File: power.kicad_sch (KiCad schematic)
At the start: 17 parts, among them J1 Conn_01x02, U2 TPS563200

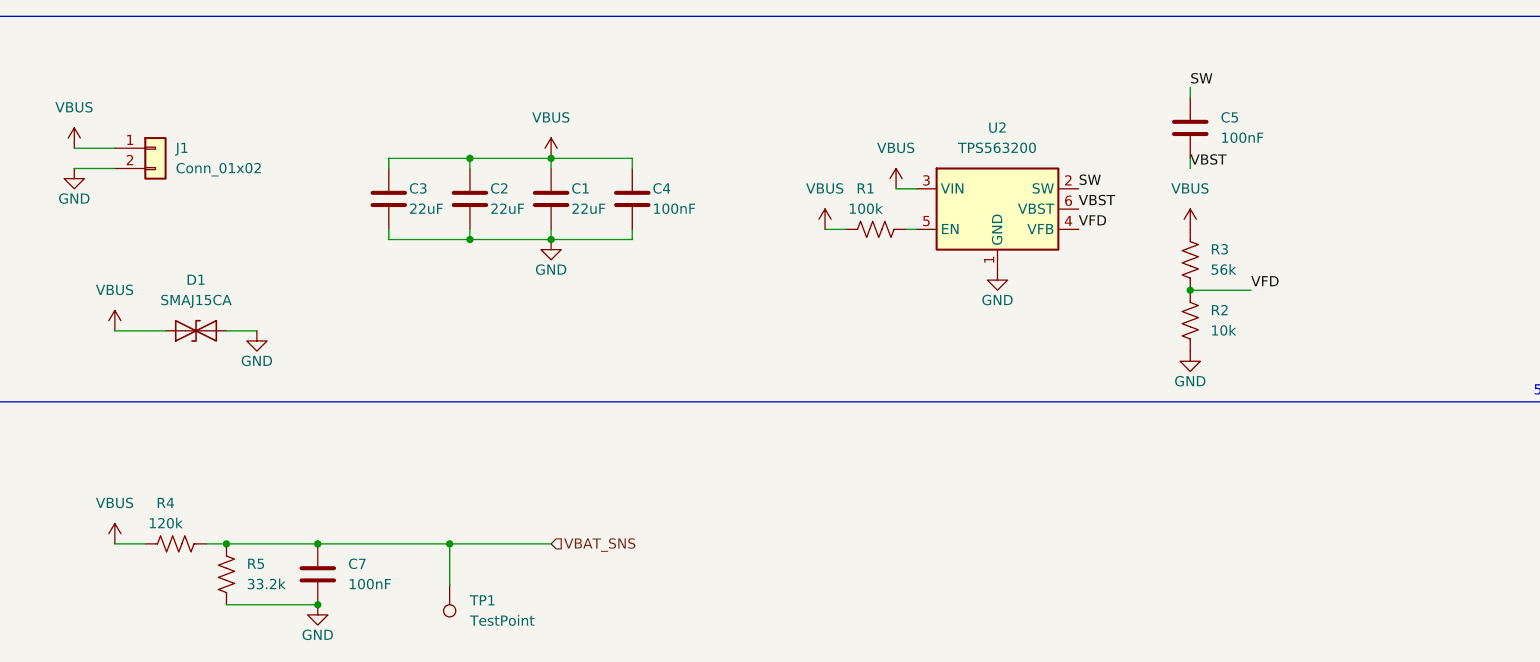
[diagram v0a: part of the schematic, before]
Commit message: fix power schematic and decide to just do undervolt protection in software
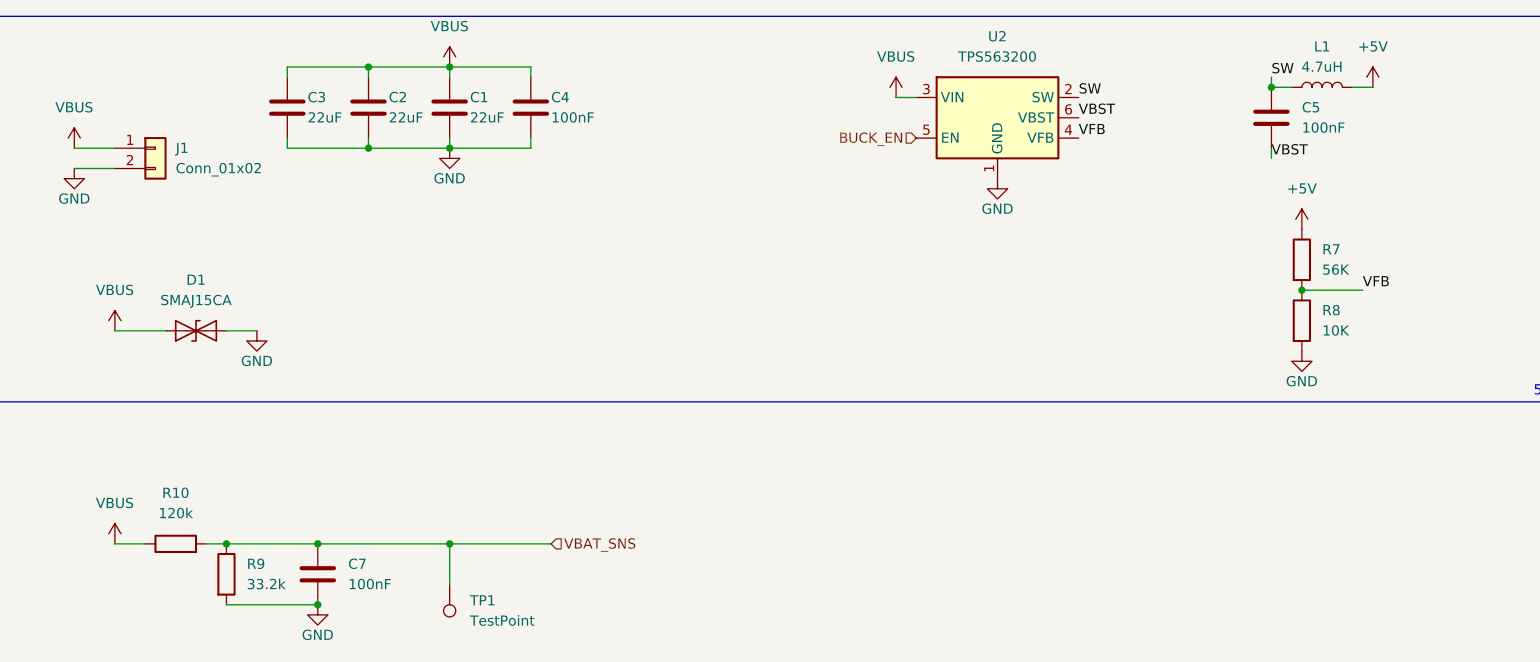
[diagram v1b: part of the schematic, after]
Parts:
- removed R1: 100k, PCM_SparkFun-Resistor:R_0603_1608Metric, symbol PCM_SparkFun-Resistor:R
- removed R2: 10k, PCM_SparkFun-Resistor:R_0603_1608Metric, symbol PCM_SparkFun-Resistor:R
- removed R3: 56k, PCM_SparkFun-Resistor:R_0603_1608Metric, symbol PCM_SparkFun-Resistor:R
- removed R4: 120k, PCM_SparkFun-Resistor:R_0603_1608Metric, symbol PCM_SparkFun-Resistor:R
- removed R5: 33.2k, PCM_SparkFun-Resistor:R_0603_1608Metric, symbol PCM_SparkFun-Resistor:R
- added L1: 4.7uH, symbol Device:L
- added R10: 120k, symbol Device:R
- added R7: 56K, symbol Device:R
- added R8: 10K, symbol Device:R
- added R9: 33.2k, symbol Device:R
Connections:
- net +5V: now also L1.2, R7.1
- net GND: now also R8.2, R9.2
- net SW: now also L1.1
- net VBAT_SNS: now also R10.2, R9.1
- net VBUS: now also R10.1
- net BUCK_EN: now reaches U2.5 (EN)
- net VFD renamed VFB
- net VFB: now also R7.2, R8.1
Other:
- title: (none) -> BeetleBoard Power
- moved on the sheet: C1, C2, C3, C4, C5, U2

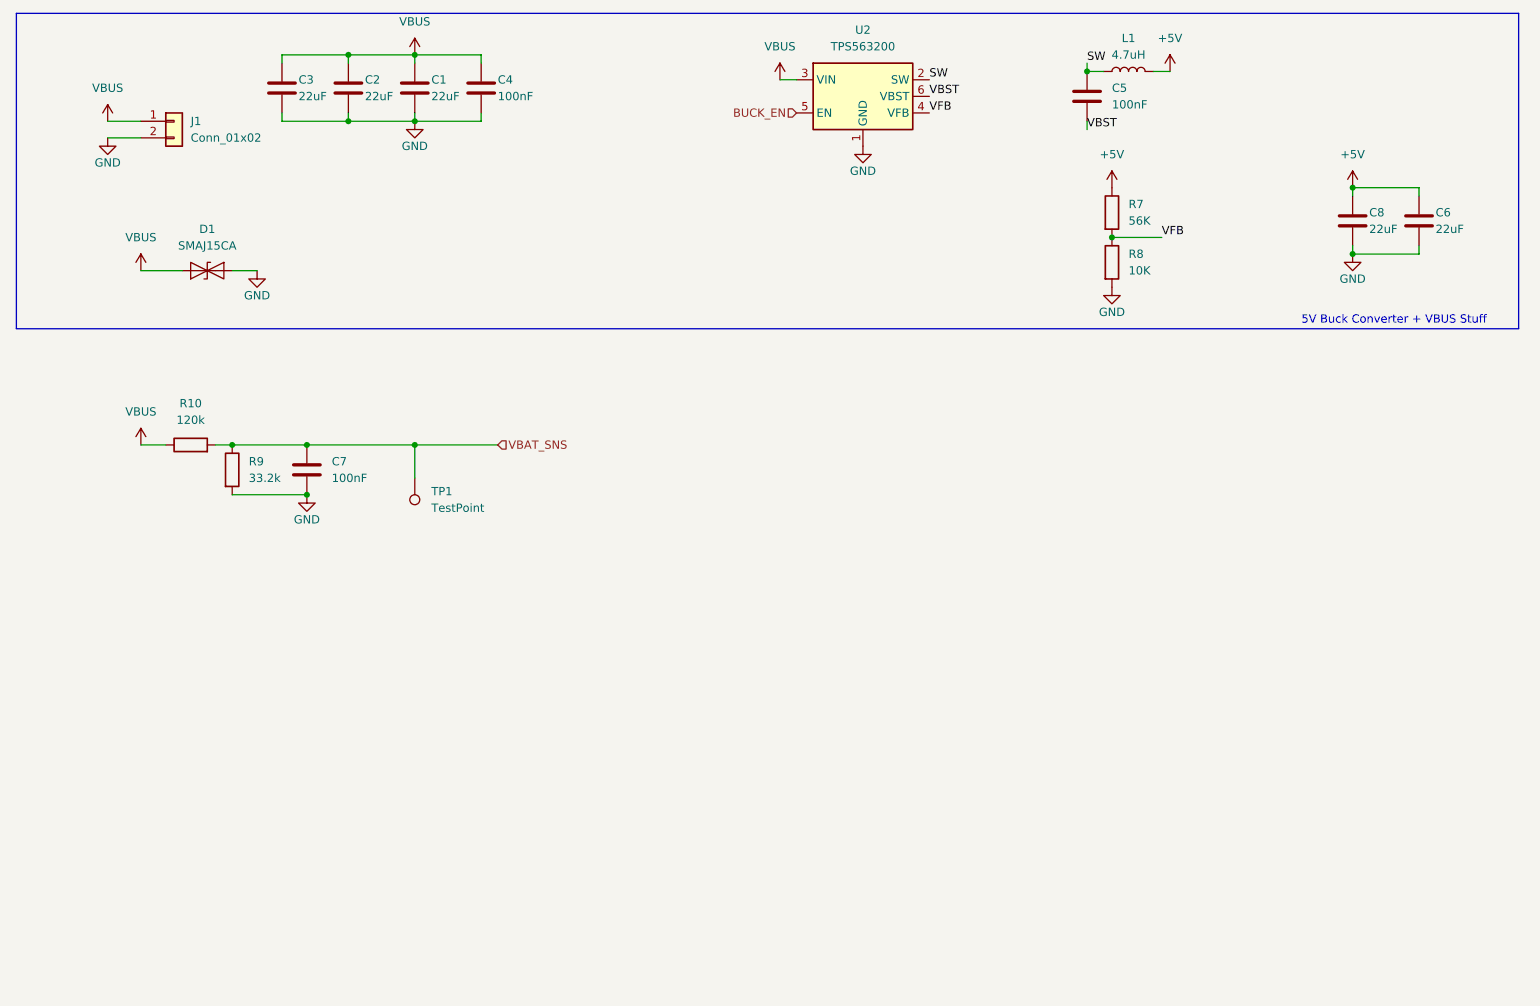
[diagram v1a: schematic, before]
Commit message: add ESC Ports
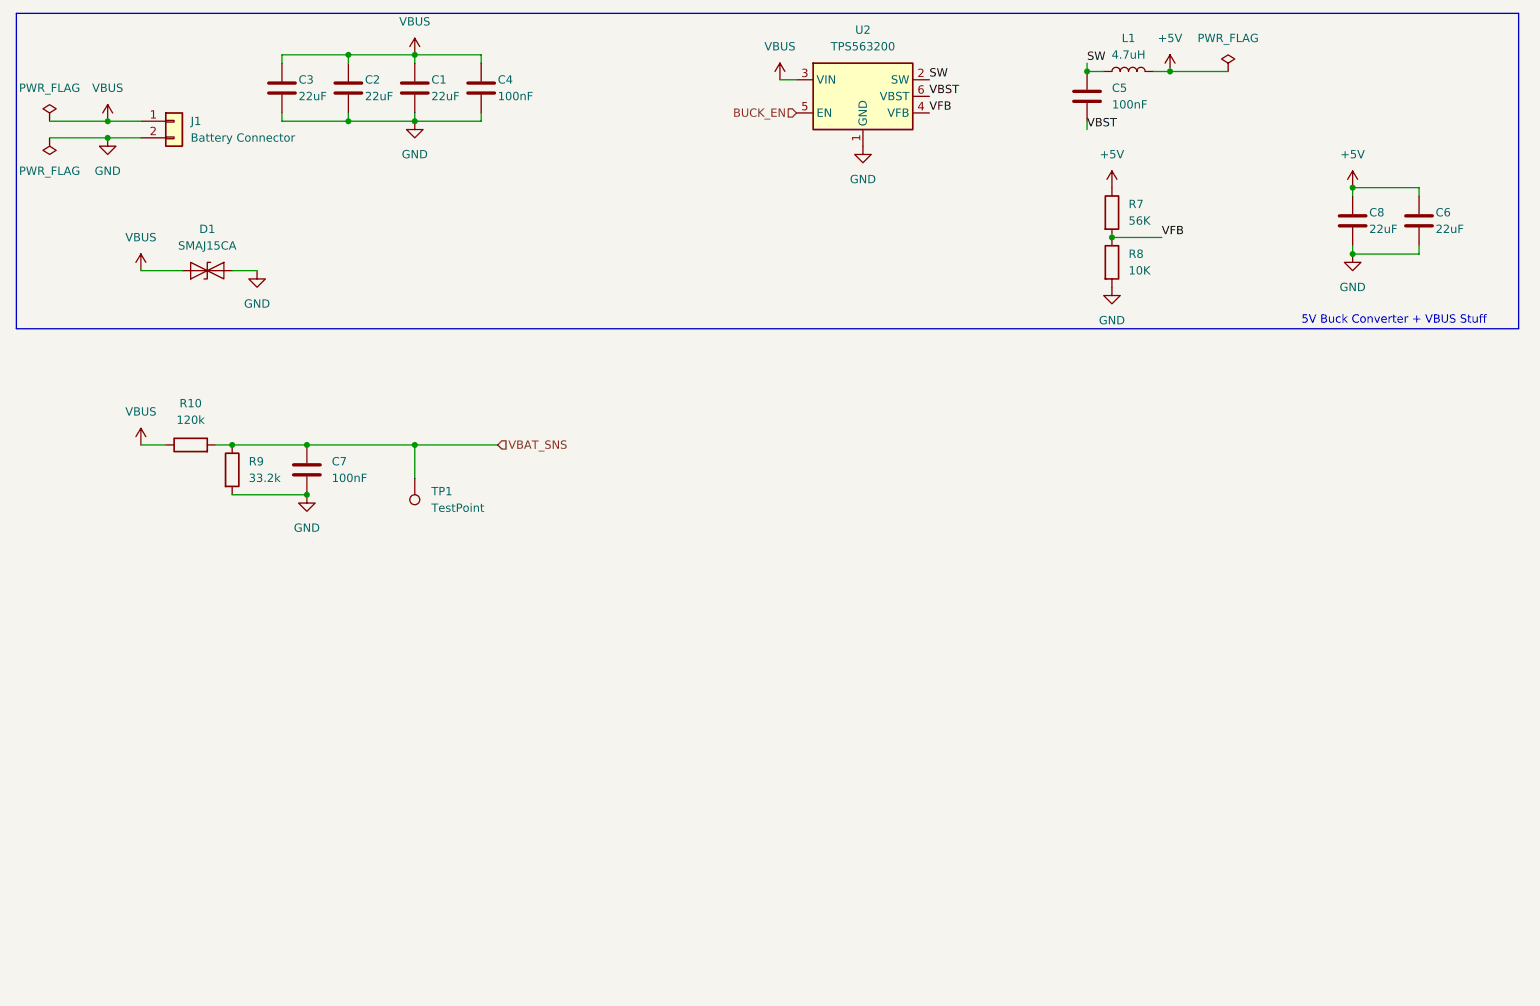
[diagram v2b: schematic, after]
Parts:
- J1: value Conn_01x02 -> Battery Connector

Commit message: add IMU
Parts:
- added TP2, TP3, TP4: TestPoint, symbol Connector:TestPoint
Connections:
- net +5V: now also TP2.1
- net GND: now also TP3.1
- new net +3V3: TP4.1

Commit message: fix power distrubution
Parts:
- removed D1: SMAJ15CA, Diode_SMD:D_SMA, symbol Diode:SMAJ15CA
- added D1: SMAJ40CA, Diode_SMD:D_SMA, symbol Diode:SMAJ40CA
- added J10: VBAT_ESC_C, symbol Connector_Generic:Conn_01x02
- added J11: VBAT_ESC_E, symbol Connector_Generic:Conn_01x02
- added J12: VBAT_ESC_F, symbol Connector_Generic:Conn_01x02
- added J13: VBAT_ESC_G, symbol Connector_Generic:Conn_01x02
- added J14: VBAT_ESC_D, symbol Connector_Generic:Conn_01x02
- added J15: VBAT_ESC_H, symbol Connector_Generic:Conn_01x02
- added J8: VBAT_ESC_A, symbol Connector_Generic:Conn_01x02
- added J9: VBAT_ESC_B, symbol Connector_Generic:Conn_01x02
- added SW1: FingerTech Switch, symbol Switch:SW_SPST
- added TP5: TestPoint, symbol Connector:TestPoint
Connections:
- net GND: now also D1.2 (A2), J10.2 (Pin_2), J11.2 (Pin_2), J12.2 (Pin_2), J13.2 (Pin_2), J14.2 (Pin_2), J15.2 (Pin_2), J8.2 (Pin_2), J9.2 (Pin_2)
- net VBUS: now also D1.1 (A1), J10.1 (Pin_1), J11.1 (Pin_1), J12.1 (Pin_1), J13.1 (Pin_1), J14.1 (Pin_1), J15.1 (Pin_1), J8.1 (Pin_1), J9.1 (Pin_1), SW1.1 (A), TP5.1; no longer J1.1 (Pin_1)
- new net: J1.1 (Pin_1), SW1.2 (B)
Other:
- moved on the sheet: C1, C2, C3, C4, J1

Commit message: add ELRS Reciever and clean up some stuff
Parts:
- TP1: value TestPoint -> TP_VBAT_SNS
- TP2: value TestPoint -> TP_5V
- TP3: value TestPoint -> TP_GND
- TP4: value TestPoint -> TP_3V3
- TP5: value TestPoint -> TP_VBAT(VBUS)
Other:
- note added: "Battery Voltage Sensing"
- note added: "Power Distrubution"
- note added: "Test Points"
- moved on the sheet: TP2, TP3, TP4, TP5
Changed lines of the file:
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@@
 	)
 	(rectangle
-		(start 199.39 67.31)
+		(start 196.85 67.31)
 		(end 264.16 104.14)
 		(stroke
@@
 		)
 	)
+	(text "Battery Voltage Sensing"
+		(exclude_from_sim no)
+		(at 113.03 104.14 0)
+		(effects
+			(font
+				(size 1.27 1.27)
+			)
+		)
+	)
 	(text "5V Buck Converter + VBUS Stuff"
 		(exclude_from_sim no)
@@
 		)
 	)
+	(text "Test Points"
+		(exclude_from_sim no)
+		(at 257.81 102.87 0)
+		(effects
+			(font
+				(size 1.27 1.27)
+			)
+		)
+	)
+	(text "Power Distrubution"
+		(exclude_from_sim no)
+		(at 115.57 163.83 0)
+		(effects
+			(font
+				(size 1.27 1.27)
+			)
+		)
+	)
 	(junction
 		(at 62.23 35.56)
@@
 	(wire
 		(pts
-			(xy 250.19 78.74) (xy 250.19 85.09)
+			(xy 246.38 78.74) (xy 246.38 85.09)
 		)
 		(stroke
@@
 	(wire
 		(pts
-			(xy 220.98 78.74) (xy 220.98 85.09)
+			(xy 217.17 78.74) (xy 217.17 85.09)
 		)
 		(stroke
@@
 	(wire
 		(pts
-			(xy 204.47 78.74) (xy 204.47 85.09)
+			(xy 200.66 78.74) (xy 200.66 85.09)
 		)
 		(stroke
@@
 	(wire
 		(pts
-			(xy 236.22 78.74) (xy 236.22 85.09)
+			(xy 232.41 78.74) (xy 232.41 85.09)
 		)
 		(stroke
@@
 	(symbol
 		(lib_id "power:GND")
-		(at 220.98 78.74 180)
+		(at 217.17 78.74 180)
 		(unit 1)
 		(body_style 1)
@@
 		(fields_autoplaced yes)
 		(property "Reference" "#PWR015"
-			(at 220.98 72.39 0)
+			(at 217.17 72.39 0)
 			(hide yes)
 			(show_name no)
@@
 		)
 		(property "Value" "GND"
-			(at 220.98 73.66 0)
+			(at 217.17 73.66 0)
 			(show_name no)
 			(do_not_autoplace no)
@@
 		)
 		(property "Footprint" ""
-			(at 220.98 78.74 0)
+			(at 217.17 78.74 0)
 			(hide yes)
 			(show_name no)
@@
 		)
 		(property "Datasheet" ""
-			(at 220.98 78.74 0)
+			(at 217.17 78.74 0)
 			(hide yes)
 			(show_name no)
@@
 		)
 		(property "Description" "Power symbol creates a global label with name \"GND\" , ground"
-			(at 220.98 78.74 0)
+			(at 217.17 78.74 0)
 			(hide yes)
 			(show_name no)
@@
 	(symbol
 		(lib_id "power:+3V3")
-		(at 236.22 78.74 0)
+		(at 232.41 78.74 0)
 		(unit 1)
 		(body_style 1)
@@
 		(fields_autoplaced yes)
 		(property "Reference" "#PWR016"
-			(at 236.22 82.55 0)
+			(at 232.41 82.55 0)
 			(hide yes)
 			(show_name no)
@@
 		)
 		(property "Value" "+3V3"
-			(at 236.22 73.66 0)
+			(at 232.41 73.66 0)
 			(show_name no)
 			(do_not_autoplace no)
@@
 		)
 		(property "Footprint" ""
-			(at 236.22 78.74 0)
+			(at 232.41 78.74 0)
 			(hide yes)
 			(show_name no)
@@
 		)
 		(property "Datasheet" ""
-			(at 236.22 78.74 0)
+			(at 232.41 78.74 0)
 			(hide yes)
 			(show_name no)
@@
 		)
 		(property "Description" "Power symbol creates a global label with name \"+3V3\""
-			(at 236.22 78.74 0)
+			(at 232.41 78.74 0)
 			(hide yes)
 			(show_name no)
@@
 	(symbol
 		(lib_id "power:+5V")
-		(at 204.47 78.74 0)
+		(at 200.66 78.74 0)
 		(unit 1)
 		(body_style 1)
@@
 		(fields_autoplaced yes)
 		(property "Reference" "#PWR013"
-			(at 204.47 82.55 0)
+			(at 200.66 82.55 0)
 			(hide yes)
 			(show_name no)
@@
 		)
 		(property "Value" "+5V"
-			(at 204.47 73.66 0)
+			(at 200.66 73.66 0)
 			(show_name no)
 			(do_not_autoplace no)
@@
 		)
 		(property "Footprint" ""
-			(at 204.47 78.74 0)
+			(at 200.66 78.74 0)
 			(hide yes)
 			(show_name no)
@@
 		)
 		(property "Datasheet" ""
-			(at 204.47 78.74 0)
+			(at 200.66 78.74 0)
 			(hide yes)
 			(show_name no)
@@
 		)
 		(property "Description" "Power symbol creates a global label with name \"+5V\""
-			(at 204.47 78.74 0)
+			(at 200.66 78.74 0)
 			(hide yes)
 			(show_name no)
@@
 	(symbol
 		(lib_id "Connector:TestPoint")
-		(at 220.98 85.09 180)
+		(at 217.17 85.09 180)
 		(unit 1)
 		(body_style 1)
@@
 		(fields_autoplaced yes)
 		(property "Reference" "TP3"
-			(at 223.52 87.1219 0)
+			(at 219.71 87.1219 0)
 			(show_name no)
 			(do_not_autoplace no)
@@
 			)
 		)
-		(property "Value" "TestPoint"
-			(at 223.52 89.6619 0)
+		(property "Value" "TP_GND"
+			(at 219.71 89.6619 0)
 			(show_name no)
 			(do_not_autoplace no)
@@
 		)
 		(property "Footprint" ""
-			(at 215.9 85.09 0)
+			(at 212.09 85.09 0)
 			(hide yes)
 			(show_name no)
@@
 		)
 		(property "Datasheet" ""
-			(at 215.9 85.09 0)
+			(at 212.09 85.09 0)
 			(hide yes)
 			(show_name no)
@@
 		)
 		(property "Description" "test point"
-			(at 220.98 85.09 0)
+			(at 217.17 85.09 0)
 			(hide yes)
 			(show_name no)
@@
 			)
 		)
-		(property "Value" "TestPoint"
+		(property "Value" "TP_VBAT_SNS"
 			(at 97.79 92.2019 0)
 			(show_name no)
@@
 	(symbol
 		(lib_id "power:VBUS")
-		(at 250.19 78.74 0)
+		(at 246.38 78.74 0)
 		(unit 1)
 		(body_style 1)
@@
 		(fields_autoplaced yes)
 		(property "Reference" "#PWR08"
-			(at 250.19 82.55 0)
+			(at 246.38 82.55 0)
 			(hide yes)
 			(show_name no)
@@
 		)
 		(property "Value" "VBUS"
-			(at 250.19 73.66 0)
+			(at 246.38 73.66 0)
 			(show_name no)
 			(do_not_autoplace no)
@@
 		)
 		(property "Footprint" ""
-			(at 250.19 78.74 0)
+			(at 246.38 78.74 0)
 			(hide yes)
 			(show_name no)
@@
 		)
 		(property "Datasheet" ""
-			(at 250.19 78.74 0)
+			(at 246.38 78.74 0)
 			(hide yes)
 			(show_name no)
@@
 		)
 		(property "Description" "Power symbol creates a global label with name \"VBUS\""
-			(at 250.19 78.74 0)
+			(at 246.38 78.74 0)
 			(hide yes)
 			(show_name no)
@@
 	(symbol
 		(lib_id "Connector:TestPoint")
-		(at 250.19 85.09 180)
+		(at 246.38 85.09 180)
 		(unit 1)
 		(body_style 1)
@@
 		(fields_autoplaced yes)
 		(property "Reference" "TP5"
-			(at 252.73 87.1219 0)
+			(at 248.92 87.1219 0)
 			(show_name no)
 			(do_not_autoplace no)
@@
 			)
 		)
-		(property "Value" "TestPoint"
-			(at 252.73 89.6619 0)
+		(property "Value" "TP_VBAT(VBUS)"
+			(at 248.92 89.6619 0)
 			(show_name no)
 			(do_not_autoplace no)
@@
 		)
 		(property "Footprint" ""
-			(at 245.11 85.09 0)
+			(at 241.3 85.09 0)
 			(hide yes)
 			(show_name no)
@@
 		)
 		(property "Datasheet" ""
-			(at 245.11 85.09 0)
+			(at 241.3 85.09 0)
 			(hide yes)
 			(show_name no)
@@
 		)
 		(property "Description" "test point"
-			(at 250.19 85.09 0)
+			(at 246.38 85.09 0)
 			(hide yes)
 			(show_name no)
@@
 	(symbol
 		(lib_id "Connector:TestPoint")
-		(at 204.47 85.09 180)
+		(at 200.66 85.09 180)
 		(unit 1)
 		(body_style 1)
@@
 		(fields_autoplaced yes)
 		(property "Reference" "TP2"
-			(at 207.01 87.1219 0)
+			(at 203.2 87.1219 0)
 			(show_name no)
 			(do_not_autoplace no)
@@
 			)
 		)
-		(property "Value" "TestPoint"
-			(at 207.01 89.6619 0)
+		(property "Value" "TP_5V"
+			(at 203.2 89.6619 0)
 			(show_name no)
 			(do_not_autoplace no)
@@
 		)
 		(property "Footprint" ""
-			(at 199.39 85.09 0)
+			(at 195.58 85.09 0)
 			(hide yes)
 			(show_name no)
@@
 		)
 		(property "Datasheet" ""
-			(at 199.39 85.09 0)
+			(at 195.58 85.09 0)
 			(hide yes)
 			(show_name no)
@@
 		)
 		(property "Description" "test point"
-			(at 204.47 85.09 0)
+			(at 200.66 85.09 0)
 			(hide yes)
 			(show_name no)
@@
 	(symbol
 		(lib_id "Connector:TestPoint")
-		(at 236.22 85.09 180)
+		(at 232.41 85.09 180)
 		(unit 1)
 		(body_style 1)
@@
 		(fields_autoplaced yes)
 		(property "Reference" "TP4"
-			(at 238.76 87.1219 0)
+			(at 234.95 87.1219 0)
 			(show_name no)
 			(do_not_autoplace no)
@@
 			)
 		)
-		(property "Value" "TestPoint"
-			(at 238.76 89.6619 0)
+		(property "Value" "TP_3V3"
+			(at 234.95 89.6619 0)
 			(show_name no)
 			(do_not_autoplace no)
@@
 		)
 		(property "Footprint" ""
-			(at 231.14 85.09 0)
+			(at 227.33 85.09 0)
 			(hide yes)
 			(show_name no)
@@
 		)
 		(property "Datasheet" ""
-			(at 231.14 85.09 0)
+			(at 227.33 85.09 0)
 			(hide yes)
 			(show_name no)
@@
 		)
 		(property "Description" "test point"
-			(at 236.22 85.09 0)
+			(at 232.41 85.09 0)
 			(hide yes)
 			(show_name no)
